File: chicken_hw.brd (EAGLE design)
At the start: 25.7 x 38.1 mm, 13 parts

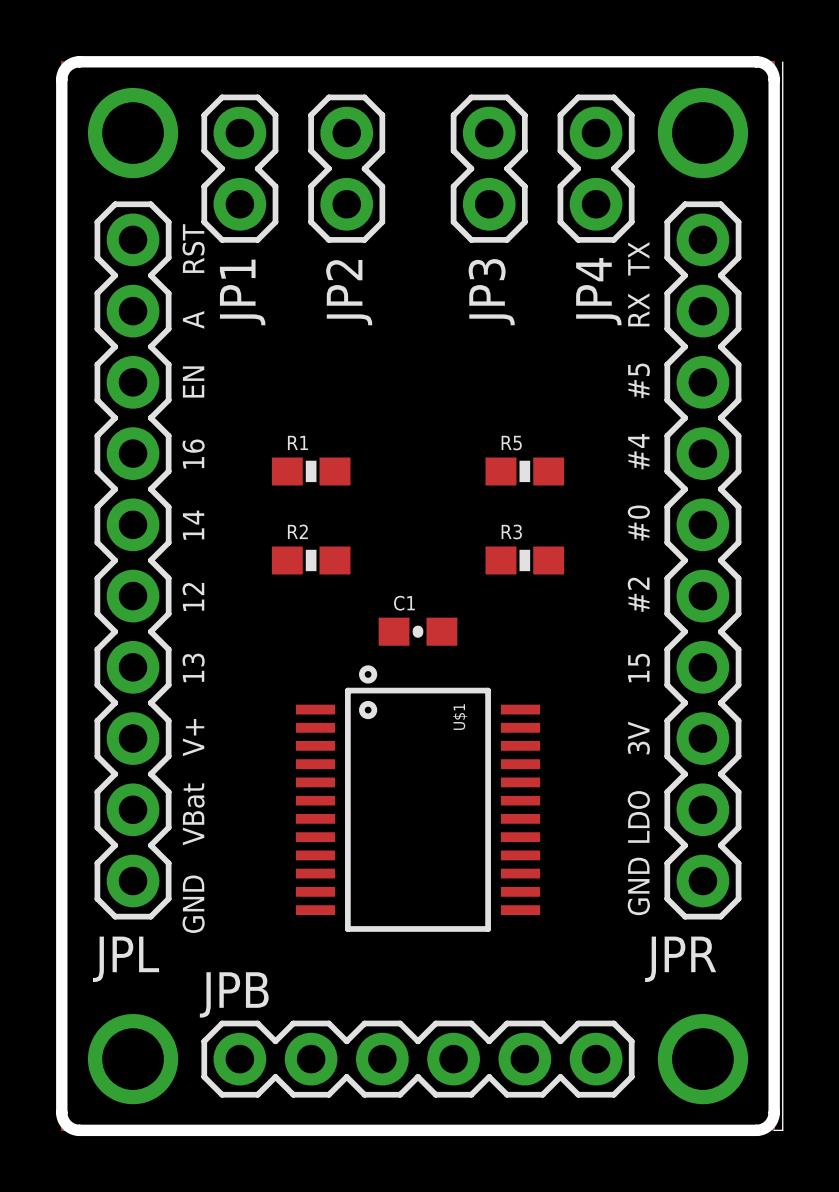
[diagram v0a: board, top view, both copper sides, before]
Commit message: First complete routing of board, 2 vias
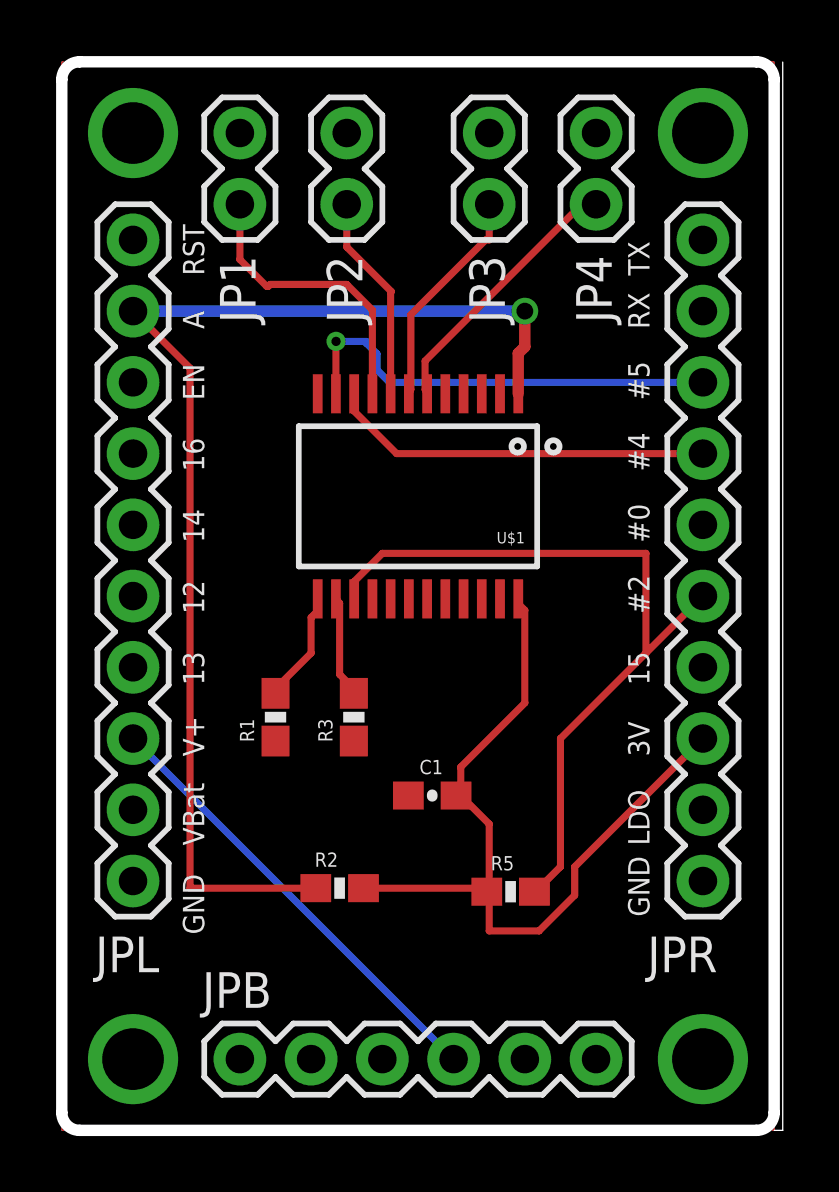
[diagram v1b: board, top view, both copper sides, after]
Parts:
- moved R5 15.0 mm to (16.0, 8.51), turned to 180 degrees
- moved R2 11.7 mm to (9.91, 8.64)
- moved U$1 11.2 mm to (12.7, 22.6), turned to 180 degrees
- moved R1 8.85 mm to (7.62, 14.7), turned to 90 degrees
- moved R3 8.27 mm to (10.4, 14.7), turned to 90 degrees
- moved C1 5.86 mm to (13.2, 11.9), turned to 180 degrees
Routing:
- net A: track 0.00 -> 42.9 mm, vias 0 -> 1
- net 3.3V: track 0.00 -> 29.0 mm
- net EN_MUX: track 0.00 -> 28.0 mm
- net VPLUS: track 0.00 -> 16.2 mm
- net GPIO5: track 0.00 -> 15.9 mm, vias 0 -> 1
- net GPIO4: track 0.00 -> 13.7 mm
- net N$2: track 0.00 -> 10.5 mm
- net N$5: track 0.00 -> 9.60 mm
- net N$4: track 0.00 -> 8.01 mm
- net N$3: track 0.00 -> 7.42 mm
- net N$1: track 0.00 -> 4.00 mm
- net N$6: track 0.00 -> 3.63 mm

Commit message: Add two leds to gpio 16,14 for easy status
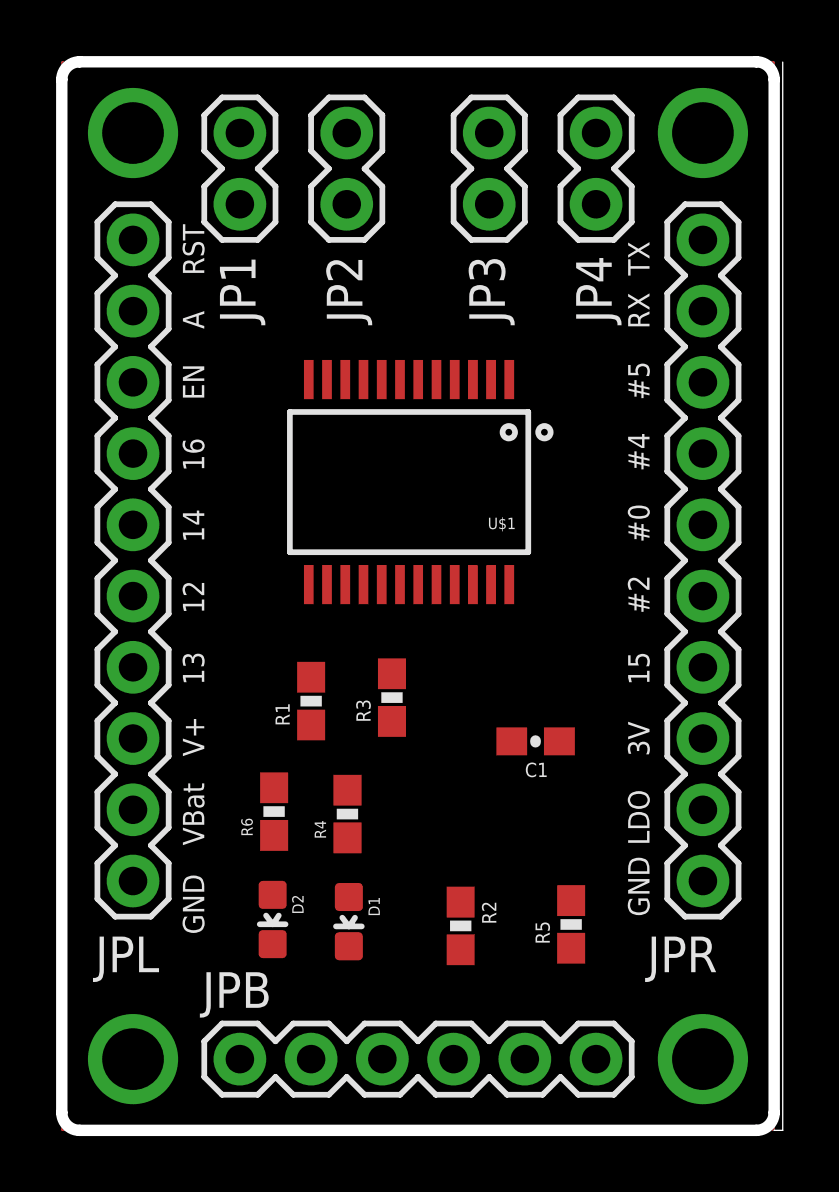
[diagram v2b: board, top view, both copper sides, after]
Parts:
- added D1, D2: GREEN, SparkFun-LED:LED-0603
- added R4, R6: 2.7k, SparkFun-Resistors:0603-RES
- moved R2 4.52 mm to (14.2, 7.29), turned to 270 degrees
- moved C1 4.16 mm to (16.9, 13.9), turned to 0 degrees
- moved R5 2.45 mm to (18.2, 7.34), turned to 270 degrees
- moved R3 1.53 mm to (11.8, 15.4)
- moved R1 1.39 mm to (8.89, 15.3)
- moved U$1 0.60 mm to (12.4, 23.1)
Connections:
- new net N$8: D1.A, R4.1
- new net N$9: D2.A, R6.1
- net GND: now also D1.C, D2.C
- net GPIO14: now also R6.2
- net GPIO16: now also R4.2
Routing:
- net A: track 42.9 -> 0.00 mm, vias 1 -> 0
- net 3.3V: track 29.0 -> 0.00 mm
- net EN_MUX: track 28.0 -> 0.00 mm
- net VPLUS: track 16.2 -> 0.00 mm
- net GPIO5: track 15.9 -> 0.00 mm, vias 1 -> 0
- net GPIO4: track 13.7 -> 0.00 mm
- net N$2: track 10.5 -> 0.00 mm
- net N$5: track 9.60 -> 0.00 mm
- net N$4: track 8.01 -> 0.00 mm
- net N$3: track 7.42 -> 0.00 mm
- net N$1: track 4.00 -> 0.00 mm
- net N$6: track 3.63 -> 0.00 mm

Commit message: Finish touchup of autorouter traces manually
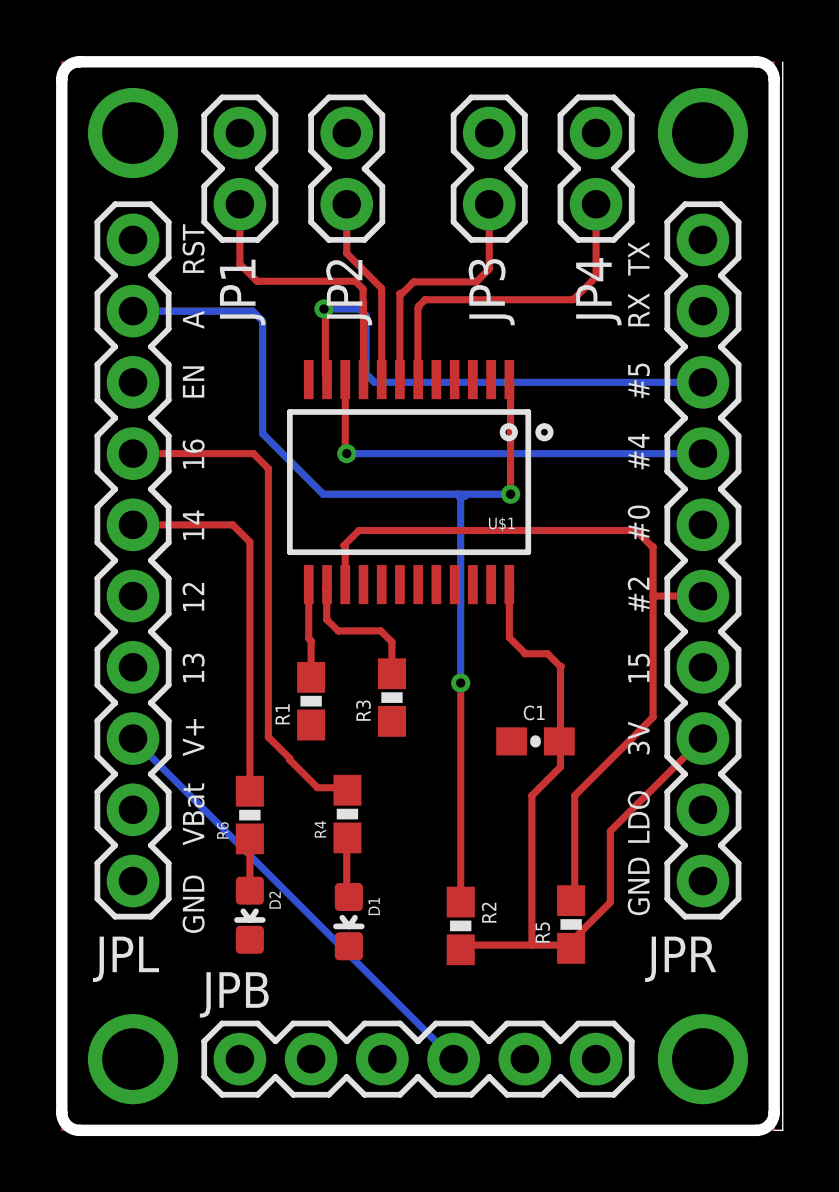
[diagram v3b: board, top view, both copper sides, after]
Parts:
- moved R6 0.87 mm to (6.71, 11.2)
- moved D2 0.83 mm to (6.71, 7.67)
- turned C1 to 180 degrees
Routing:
- net A: track 0.00 -> 37.1 mm, vias 0 -> 2
- net 3.3V: track 0.00 -> 28.3 mm
- net EN_MUX: track 0.00 -> 28.3 mm
- net GPIO5: track 0.00 -> 18.4 mm, vias 0 -> 1
- net GPIO16: track 0.00 -> 18.3 mm
- net VPLUS: track 0.00 -> 16.2 mm
- net GPIO4: track 0.00 -> 15.4 mm, vias 0 -> 1
- net GPIO14: track 0.00 -> 13.3 mm
- net N$5: track 0.00 -> 11.8 mm
- net N$2: track 0.00 -> 10.1 mm
- net N$4: track 0.00 -> 8.92 mm
- net N$3: track 0.00 -> 6.77 mm
- net N$6: track 0.00 -> 5.09 mm
- net N$1: track 0.00 -> 3.34 mm
- net N$8: track 0.00 -> 2.16 mm
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
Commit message: Add designer information and schematic frame
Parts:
- added FRAME1: FRAME-LETTER, SparkFun-Aesthetics:CREATIVE_COMMONS
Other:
- board text added: "Jason Holden jason.k.holden@gmail.com"
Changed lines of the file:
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@@
 <wire x1="0.635" y1="0" x2="0" y2="0.635" width="0.4064" layer="20" curve="-90"/>
 <wire x1="0" y1="0.635" x2="0" y2="37.465" width="0.4064" layer="20"/>
+<text x="28.0924" y="-13.2334" size="1.778" layer="51">Jason Holden
+jason.k.holden@gmail.com</text>
 </plain>
 <attributes>
@@
 <attribute name="VALUE" x="7.8486" y="10.2235" size="0.4064" layer="27" font="vector" ratio="12" rot="R90"/>
 </element>
+<element name="FRAME1" library="SparkFun-Aesthetics" package="CREATIVE_COMMONS" value="FRAME-LETTER" x="-3.937" y="-9.6012" smashed="yes"/>
 </elements>
 <signals>
@@
 </board>
 </drawing>
+<compatibility>
+<note version="6.3" minversion="6.2.2" severity="warning">
+Since Version 6.2.2 text objects can contain more than one line,
+which will not be processed correctly with this version.
+</note>
+</compatibility>
 </eagle>

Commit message: Add open source hardware logo and bottom silk
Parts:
- added LOGO1: OSHW-LOGOS, SparkFun-Aesthetics:OSHW-LOGO-S
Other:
- board text added: "4-input Temp Sensor jason.k.holden@gmail.com ver 0.1 11-8-2015"
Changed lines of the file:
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@@
 <grid distance="0.001" unitdist="inch" unit="inch" style="dots" multiple="1" display="yes" altdistance="0.025" altunitdist="inch" altunit="inch"/>
 <layers>
-<layer number="1" name="Top" color="4" fill="1" visible="yes" active="yes"/>
-<layer number="16" name="Bottom" color="1" fill="1" visible="yes" active="yes"/>
+<layer number="1" name="Top" color="4" fill="1" visible="no" active="yes"/>
+<layer number="16" name="Bottom" color="1" fill="1" visible="no" active="yes"/>
 <layer number="17" name="Pads" color="2" fill="1" visible="yes" active="yes"/>
 <layer number="18" name="Vias" color="2" fill="1" visible="yes" active="yes"/>
@@
 <text x="28.0924" y="-13.2334" size="1.778" layer="51">Jason Holden
 jason.k.holden@gmail.com</text>
+<text x="12.6492" y="19.1516" size="1.016" layer="22" font="vector" ratio="12" rot="MR90" align="center">4-input Temp Sensor
+jason.k.holden@gmail.com
+ver 0.1 11-8-2015</text>
 </plain>
 <attributes>
@@
 </element>
 <element name="FRAME1" library="SparkFun-Aesthetics" package="CREATIVE_COMMONS" value="FRAME-LETTER" x="-3.937" y="-9.6012" smashed="yes"/>
+<element name="LOGO1" library="SparkFun-Aesthetics" package="OSHW-LOGO-S" value="OSHW-LOGOS" x="18.161" y="17.4752" rot="R90"/>
 </elements>
 <signals>
